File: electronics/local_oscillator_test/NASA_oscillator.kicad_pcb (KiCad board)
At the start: 2 copper layers, 2 parts, among them U1 CE3520K3

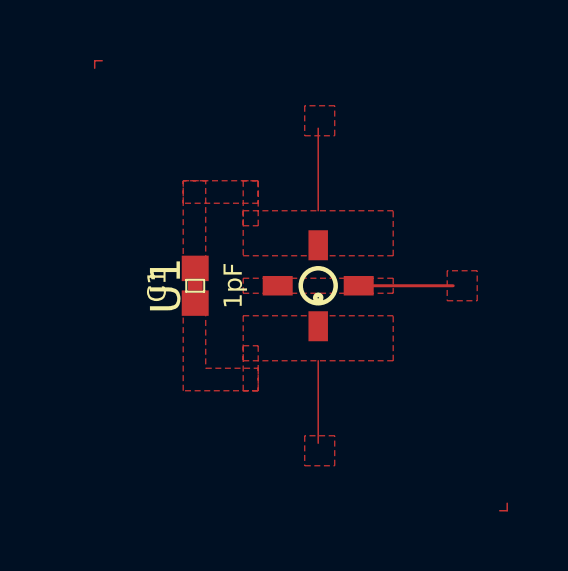
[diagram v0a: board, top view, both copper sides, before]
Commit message: Fixed boundary issue
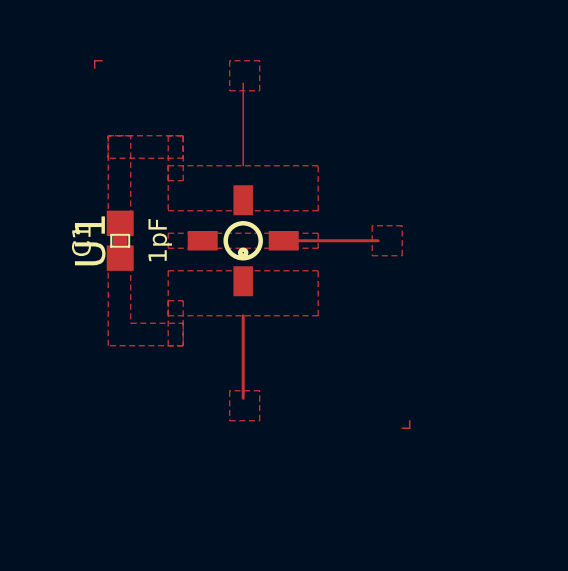
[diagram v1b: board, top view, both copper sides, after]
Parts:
- moved C1 2.92 mm to (15.8, 18.5)
- moved U1 2.92 mm to (19.9, 18.5)
